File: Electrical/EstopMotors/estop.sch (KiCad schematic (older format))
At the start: 23 parts, among them Q1 IRF9530N, Q2 IRF9530N, Q3 IRF9530N, Q4 IRF9530N

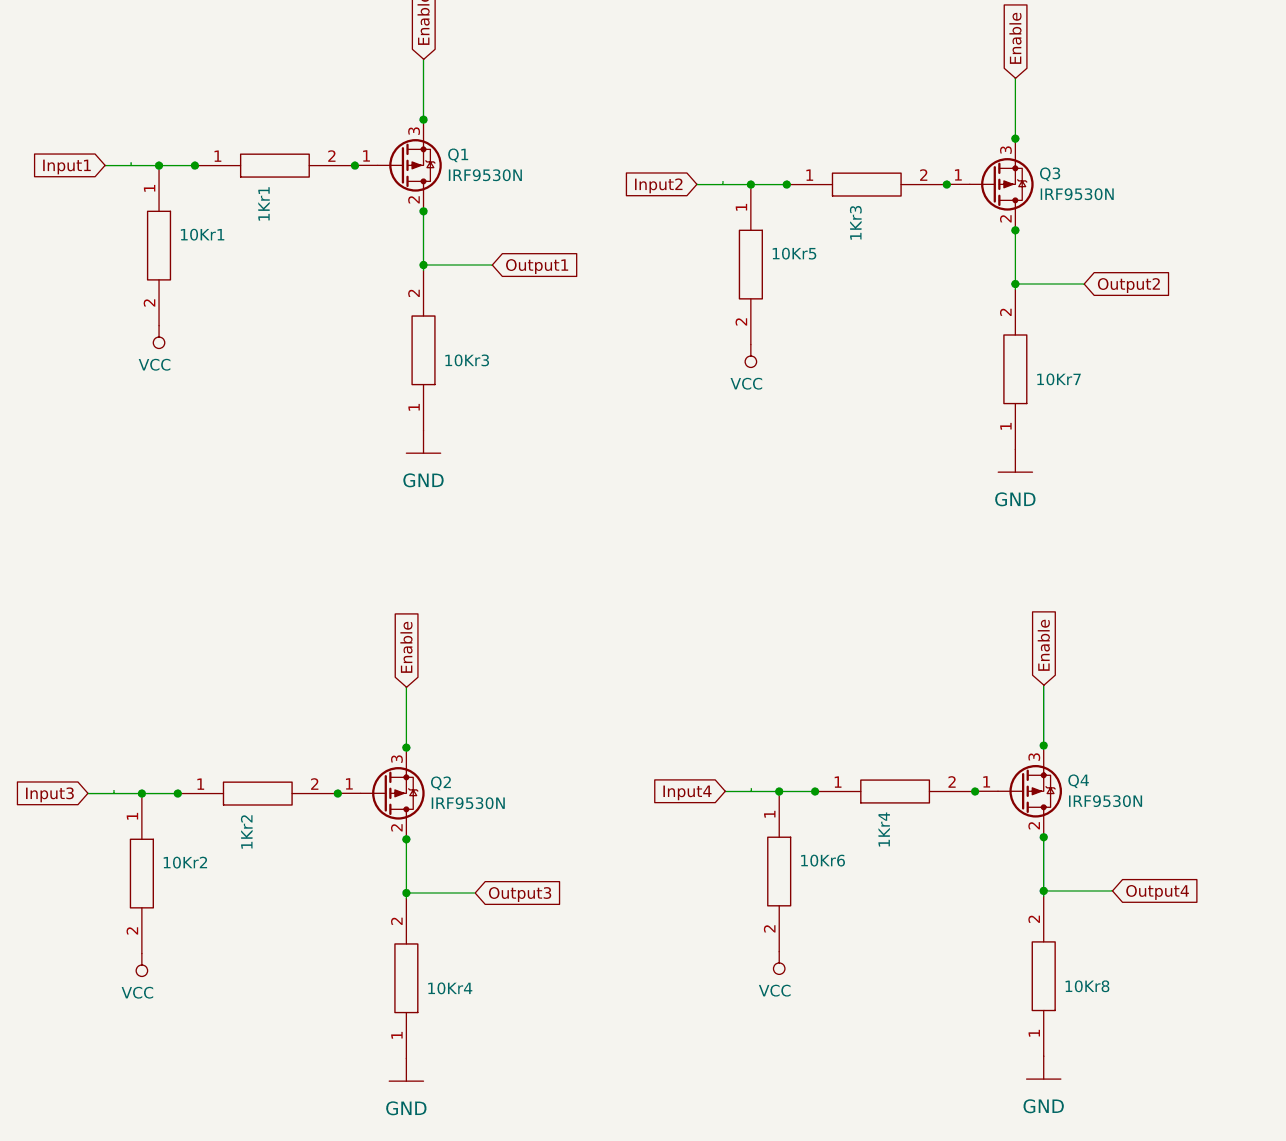
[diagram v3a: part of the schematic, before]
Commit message: updated to rev 3 and added correct designators. Uploaded rev 3 schematic
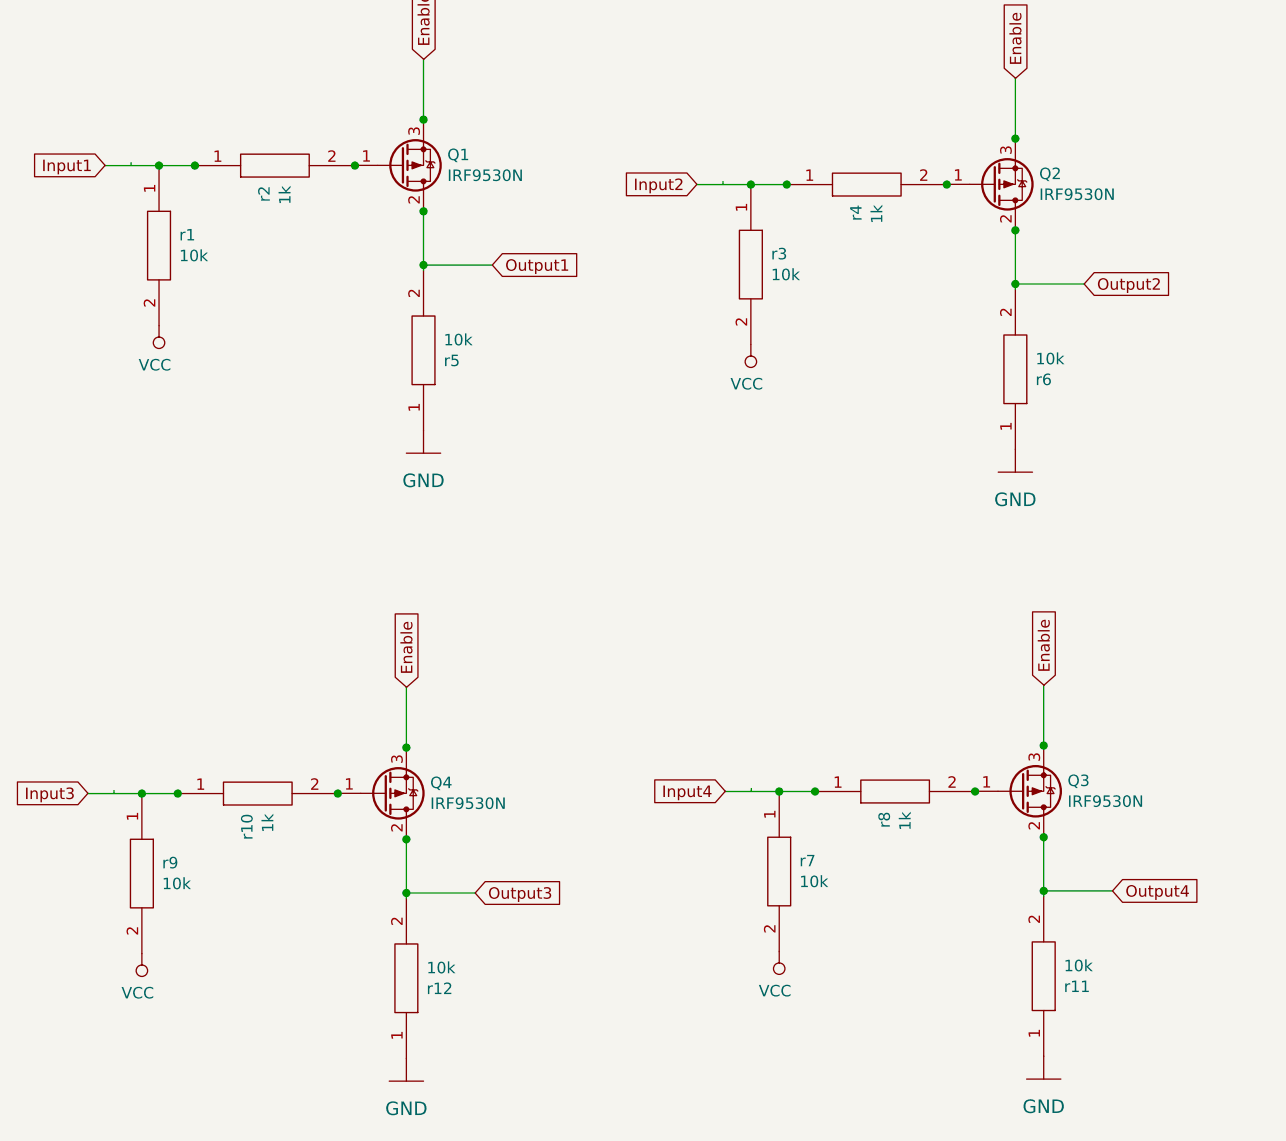
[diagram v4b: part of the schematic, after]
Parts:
- r1: renamed from 10Kr1; value ROX5SSJ1K8 -> 10k
- r10: renamed from 1Kr2; value ROX5SSJ1K8 -> 1k
- r11: renamed from 10Kr8; value ROX5SSJ1K8 -> 10k
- r12: renamed from 10Kr4; value ROX5SSJ1K8 -> 10k
- r2: renamed from 1Kr1; value ROX5SSJ1K8 -> 1k
- r3: renamed from 10Kr5; value ROX5SSJ1K8 -> 10k
- r4: renamed from 1Kr3; value ROX5SSJ1K8 -> 1k
- r5: renamed from 10Kr3; value ROX5SSJ1K8 -> 10k
- r6: renamed from 10Kr7; value ROX5SSJ1K8 -> 10k
- r7: renamed from 10Kr6; value ROX5SSJ1K8 -> 10k
- r8: renamed from 1Kr4; value ROX5SSJ1K8 -> 1k
- r9: renamed from 10Kr2; value ROX5SSJ1K8 -> 10k
- renumbered Q3 to Q2, Q4 to Q3, Q2 to Q4
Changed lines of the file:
@@
 Title "Estop"
 Date ""
-Rev "V3"
+Rev "Rev 3"
 Comp "Tyler Julian (Sooner Competitive Robotics)"
 Comment1 ""
@@
 $EndComp
 $Comp
-L estop-rescue:GND-Adafruit_Feather_M0_RFMxx-eagle-import #GND05
+L estop-rescue:GND-Adafruit_Feather_M0_RFMxx-eagle-import #GND03
 U 1 1 5DE79EBA
 P 7345 5750
-F 0 "#GND05" H 7345 5750 50  0001 C CNN
+F 0 "#GND03" H 7345 5750 50  0001 C CNN
 F 1 "GND" V 7345 5681 59  0000 R CNN
 F 2 "" H 7345 5750 50  0001 C CNN
@@
 	1171 2163 1171 2175
 $Comp
-L estop-rescue:ROX5SSJ1K8-USBhUB 1Kr1
+L estop-rescue:ROX5SSJ1K8-USBhUB r2
 U 1 1 5E4308F5
 P 1450 2176
-F 0 "1Kr1" V 1754 2264 50  0000 L CNN
-F 1 "ROX5SSJ1K8" V 1845 2264 50  0001 L CNN
+F 0 "r2" V 1754 2264 50  0000 L CNN
+F 1 "1k" V 1845 2264 50  0000 L CNN
 F 2 "Resistor_THT:R_Axial_DIN0204_L3.6mm_D1.6mm_P7.62mm_Horizontal" H 2000 2226 50  0001 L CNN
 F 3 "https://componentsearchengine.com/Datasheets/1/ROX5SSJ1K8.pdf" H 2000 2126 50  0001 L CNN
@@
 	1450 2176 1451 2176
 $Comp
-L estop-rescue:ROX5SSJ1K8-USBhUB 10Kr3
+L estop-rescue:ROX5SSJ1K8-USBhUB r5
 U 1 1 5DE69959
 P 2450 3334
-F 0 "10Kr3" V 2754 3422 50  0000 L CNN
-F 1 "ROX5SSJ1K8" V 2845 3422 50  0001 L CNN
+F 0 "r5" V 2754 3422 50  0000 L CNN
+F 1 "10k" V 2845 3422 50  0000 L CNN
 F 2 "Resistor_THT:R_Axial_DIN0204_L3.6mm_D1.6mm_P7.62mm_Horizontal" H 3000 3384 50  0001 L CNN
 F 3 "https://componentsearchengine.com/Datasheets/1/ROX5SSJ1K8.pdf" H 3000 3284 50  0001 L CNN
@@
 Connection ~ 2150 2176
 $Comp
-L estop-rescue:ROX5SSJ1K8-USBhUB 10Kr1
+L estop-rescue:ROX5SSJ1K8-USBhUB r1
 U 1 1 5E4308DE
 P 1293 2176
-F 0 "10Kr1" V 1597 2264 50  0000 L CNN
-F 1 "ROX5SSJ1K8" V 1688 2264 50  0001 L CNN
+F 0 "r1" V 1597 2264 50  0000 L CNN
+F 1 "10k" V 1688 2264 50  0000 L CNN
 F 2 "Resistor_THT:R_Axial_DIN0204_L3.6mm_D1.6mm_P7.62mm_Horizontal" H 1843 2226 50  0001 L CNN
 F 3 "https://componentsearchengine.com/Datasheets/1/ROX5SSJ1K8.pdf" H 1843 2126 50  0001 L CNN
@@
 Input2
 $Comp
-L power:VCC #PWR03
+L power:VCC #PWR02
 U 1 1 5E48F012
 P 3882 2959
-F 0 "#PWR03" H 3882 2809 50  0001 C CNN
+F 0 "#PWR02" H 3882 2809 50  0001 C CNN
 F 1 "VCC" H 3900 3132 50  0000 C CNN
 F 2 "" H 3882 2959 50  0001 C CNN
@@
 	3760 2246 3760 2258
 $Comp
-L estop-rescue:ROX5SSJ1K8-USBhUB 1Kr3
+L estop-rescue:ROX5SSJ1K8-USBhUB r4
 U 1 1 5E48F020
 P 4039 2259
-F 0 "1Kr3" V 4343 2347 50  0000 L CNN
-F 1 "ROX5SSJ1K8" V 4434 2347 50  0001 L CNN
+F 0 "r4" V 4343 2347 50  0000 L CNN
+F 1 "1k" V 4434 2347 50  0000 L CNN
 F 2 "Resistor_THT:R_Axial_DIN0204_L3.6mm_D1.6mm_P7.62mm_Horizontal" H 4589 2309 50  0001 L CNN
 F 3 "https://componentsearchengine.com/Datasheets/1/ROX5SSJ1K8.pdf" H 4589 2209 50  0001 L CNN
@@
 $EndComp
 $Comp
-L estop-rescue:GND-Adafruit_Feather_M0_RFMxx-eagle-import #GND03
+L estop-rescue:GND-Adafruit_Feather_M0_RFMxx-eagle-import #GND02
 U 1 1 5E48F026
 P 5039 3517
-F 0 "#GND03" H 5039 3517 50  0001 C CNN
+F 0 "#GND02" H 5039 3517 50  0001 C CNN
 F 1 "GND" H 5039 3396 59  0000 C CNN
 F 2 "" H 5039 3517 50  0001 C CNN
@@
 	4039 2259 4040 2259
 $Comp
-L estop-rescue:ROX5SSJ1K8-USBhUB 10Kr7
+L estop-rescue:ROX5SSJ1K8-USBhUB r6
 U 1 1 5E48F034
 P 5039 3417
-F 0 "10Kr7" V 5343 3505 50  0000 L CNN
-F 1 "ROX5SSJ1K8" V 5434 3505 50  0001 L CNN
+F 0 "r6" V 5343 3505 50  0000 L CNN
+F 1 "10k" V 5434 3505 50  0000 L CNN
 F 2 "Resistor_THT:R_Axial_DIN0204_L3.6mm_D1.6mm_P7.62mm_Horizontal" H 5589 3467 50  0001 L CNN
 F 3 "https://componentsearchengine.com/Datasheets/1/ROX5SSJ1K8.pdf" H 5589 3367 50  0001 L CNN
@@
 	5039 1794 5039 2058
 $Comp
-L Transistor_FET:IRF9540N Q3
+L Transistor_FET:IRF9540N Q2
 U 1 1 5E48F041
 P 4939 2258
-F 0 "Q3" H 5143 2212 50  0000 L CNN
+F 0 "Q2" H 5143 2212 50  0000 L CNN
 F 1 "IRF9530N" H 5143 2303 50  0000 L CNN
 F 2 "Package_TO_SOT_THT:TO-220-3_Vertical" H 5139 2183 50  0001 L CIN
@@
 Connection ~ 4739 2259
 $Comp
-L estop-rescue:ROX5SSJ1K8-USBhUB 10Kr5
+L estop-rescue:ROX5SSJ1K8-USBhUB r3
 U 1 1 5E48F058
 P 3882 2259
-F 0 "10Kr5" V 4186 2347 50  0000 L CNN
-F 1 "ROX5SSJ1K8" V 4277 2347 50  0001 L CNN
+F 0 "r3" V 4186 2347 50  0000 L CNN
+F 1 "10k" V 4277 2347 50  0000 L CNN
 F 2 "Resistor_THT:R_Axial_DIN0204_L3.6mm_D1.6mm_P7.62mm_Horizontal" H 4432 2309 50  0001 L CNN
 F 3 "https://componentsearchengine.com/Datasheets/1/ROX5SSJ1K8.pdf" H 4432 2209 50  0001 L CNN
@@
 Input3
 $Comp
-L power:VCC #PWR02
+L power:VCC #PWR04
 U 1 1 5E491333
 P 1218 5623
-F 0 "#PWR02" H 1218 5473 50  0001 C CNN
+F 0 "#PWR04" H 1218 5473 50  0001 C CNN
 F 1 "VCC" H 1236 5796 50  0000 C CNN
 F 2 "" H 1218 5623 50  0001 C CNN
@@
 	1096 4910 1096 4922
 $Comp
-L estop-rescue:ROX5SSJ1K8-USBhUB 1Kr2
+L estop-rescue:ROX5SSJ1K8-USBhUB r10
 U 1 1 5E491341
 P 1375 4923
-F 0 "1Kr2" V 1679 5011 50  0000 L CNN
-F 1 "ROX5SSJ1K8" V 1770 5011 50  0001 L CNN
+F 0 "r10" V 1679 5011 50  0000 L CNN
+F 1 "1k" V 1770 5011 50  0000 L CNN
 F 2 "Resistor_THT:R_Axial_DIN0204_L3.6mm_D1.6mm_P7.62mm_Horizontal" H 1925 4973 50  0001 L CNN
 F 3 "https://componentsearchengine.com/Datasheets/1/ROX5SSJ1K8.pdf" H 1925 4873 50  0001 L CNN
@@
 $EndComp
 $Comp
-L estop-rescue:GND-Adafruit_Feather_M0_RFMxx-eagle-import #GND02
+L estop-rescue:GND-Adafruit_Feather_M0_RFMxx-eagle-import #GND05
 U 1 1 5E491347
 P 2375 6181
-F 0 "#GND02" H 2375 6181 50  0001 C CNN
+F 0 "#GND05" H 2375 6181 50  0001 C CNN
 F 1 "GND" H 2375 6060 59  0000 C CNN
 F 2 "" H 2375 6181 50  0001 C CNN
@@
 	1375 4923 1376 4923
 $Comp
-L estop-rescue:ROX5SSJ1K8-USBhUB 10Kr4
+L estop-rescue:ROX5SSJ1K8-USBhUB r12
 U 1 1 5E491355
 P 2375 6081
-F 0 "10Kr4" V 2679 6169 50  0000 L CNN
-F 1 "ROX5SSJ1K8" V 2770 6169 50  0001 L CNN
+F 0 "r12" V 2679 6169 50  0000 L CNN
+F 1 "10k" V 2770 6169 50  0000 L CNN
 F 2 "Resistor_THT:R_Axial_DIN0204_L3.6mm_D1.6mm_P7.62mm_Horizontal" H 2925 6131 50  0001 L CNN
 F 3 "https://componentsearchengine.com/Datasheets/1/ROX5SSJ1K8.pdf" H 2925 6031 50  0001 L CNN
@@
 	2375 4458 2375 4722
 $Comp
-L Transistor_FET:IRF9540N Q2
+L Transistor_FET:IRF9540N Q4
 U 1 1 5E491362
 P 2275 4922
-F 0 "Q2" H 2479 4876 50  0000 L CNN
+F 0 "Q4" H 2479 4876 50  0000 L CNN
 F 1 "IRF9530N" H 2479 4967 50  0000 L CNN
 F 2 "Package_TO_SOT_THT:TO-220-3_Vertical" H 2475 4847 50  0001 L CIN
@@
 Connection ~ 2075 4923
 $Comp
-L estop-rescue:ROX5SSJ1K8-USBhUB 10Kr2
+L estop-rescue:ROX5SSJ1K8-USBhUB r9
 U 1 1 5E491379
 P 1218 4923
-F 0 "10Kr2" V 1522 5011 50  0000 L CNN
-F 1 "ROX5SSJ1K8" V 1613 5011 50  0001 L CNN
+F 0 "r9" V 1522 5011 50  0000 L CNN
+F 1 "10k" V 1613 5011 50  0000 L CNN
 F 2 "Resistor_THT:R_Axial_DIN0204_L3.6mm_D1.6mm_P7.62mm_Horizontal" H 1768 4973 50  0001 L CNN
 F 3 "https://componentsearchengine.com/Datasheets/1/ROX5SSJ1K8.pdf" H 1768 4873 50  0001 L CNN
@@
 Input4
 $Comp
-L power:VCC #PWR04
+L power:VCC #PWR03
 U 1 1 5E492F6C
 P 4006 5614
-F 0 "#PWR04" H 4006 5464 50  0001 C CNN
+F 0 "#PWR03" H 4006 5464 50  0001 C CNN
 F 1 "VCC" H 4024 5787 50  0000 C CNN
 F 2 "" H 4006 5614 50  0001 C CNN
@@
 	3884 4901 3884 4913
 $Comp
-L estop-rescue:ROX5SSJ1K8-USBhUB 1Kr4
+L estop-rescue:ROX5SSJ1K8-USBhUB r8
 U 1 1 5E492F7A
 P 4163 4914
-F 0 "1Kr4" V 4467 5002 50  0000 L CNN
-F 1 "ROX5SSJ1K8" V 4558 5002 50  0001 L CNN
+F 0 "r8" V 4467 5002 50  0000 L CNN
+F 1 "1k" V 4558 5002 50  0000 L CNN
 F 2 "Resistor_THT:R_Axial_DIN0204_L3.6mm_D1.6mm_P7.62mm_Horizontal" H 4713 4964 50  0001 L CNN
 F 3 "https://componentsearchengine.com/Datasheets/1/ROX5SSJ1K8.pdf" H 4713 4864 50  0001 L CNN
@@
 	4163 4914 4164 4914
 $Comp
-L estop-rescue:ROX5SSJ1K8-USBhUB 10Kr8
+L estop-rescue:ROX5SSJ1K8-USBhUB r11
 U 1 1 5E492F8E
 P 5163 6072
-F 0 "10Kr8" V 5467 6160 50  0000 L CNN
-F 1 "ROX5SSJ1K8" V 5558 6160 50  0001 L CNN
+F 0 "r11" V 5467 6160 50  0000 L CNN
+F 1 "10k" V 5558 6160 50  0000 L CNN
 F 2 "Resistor_THT:R_Axial_DIN0204_L3.6mm_D1.6mm_P7.62mm_Horizontal" H 5713 6122 50  0001 L CNN
 F 3 "https://componentsearchengine.com/Datasheets/1/ROX5SSJ1K8.pdf" H 5713 6022 50  0001 L CNN
@@
 	5163 4449 5163 4713
 $Comp
-L Transistor_FET:IRF9540N Q4
+L Transistor_FET:IRF9540N Q3
 U 1 1 5E492F9B
 P 5063 4913
-F 0 "Q4" H 5267 4867 50  0000 L CNN
+F 0 "Q3" H 5267 4867 50  0000 L CNN
 F 1 "IRF9530N" H 5267 4958 50  0000 L CNN
 F 2 "Package_TO_SOT_THT:TO-220-3_Vertical" H 5263 4838 50  0001 L CIN
@@
 Connection ~ 4863 4914
 $Comp
-L estop-rescue:ROX5SSJ1K8-USBhUB 10Kr6
+L estop-rescue:ROX5SSJ1K8-USBhUB r7
 U 1 1 5E492FB2
 P 4006 4914
-F 0 "10Kr6" V 4310 5002 50  0000 L CNN
-F 1 "ROX5SSJ1K8" V 4401 5002 50  0001 L CNN
+F 0 "r7" V 4310 5002 50  0000 L CNN
+F 1 "10k" V 4401 5002 50  0000 L CNN
 F 2 "Resistor_THT:R_Axial_DIN0204_L3.6mm_D1.6mm_P7.62mm_Horizontal" H 4556 4964 50  0001 L CNN
 F 3 "https://componentsearchengine.com/Datasheets/1/ROX5SSJ1K8.pdf" H 4556 4864 50  0001 L CNN
